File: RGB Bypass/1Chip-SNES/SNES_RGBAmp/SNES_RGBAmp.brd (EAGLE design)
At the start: 31.1 x 22.4 mm, 32 parts

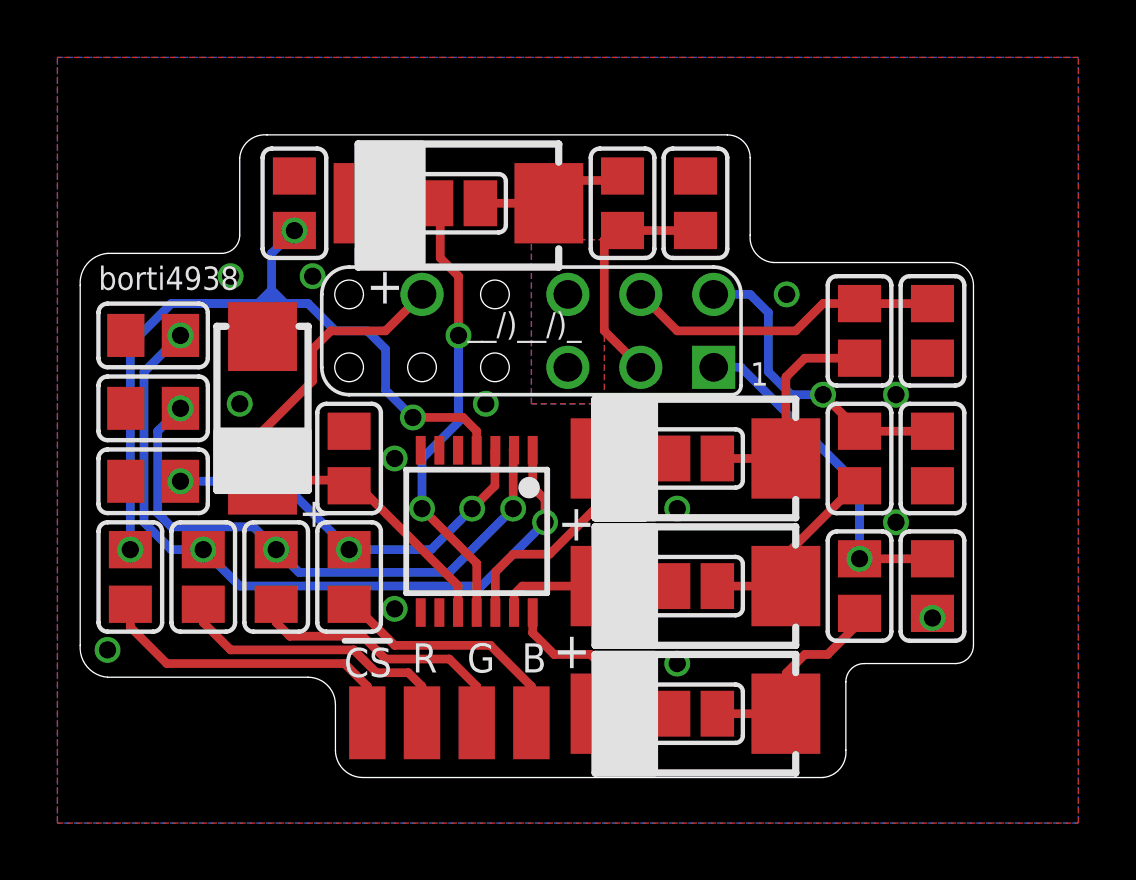
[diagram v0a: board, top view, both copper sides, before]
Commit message: rename folders a bit, add thermals to GND pads
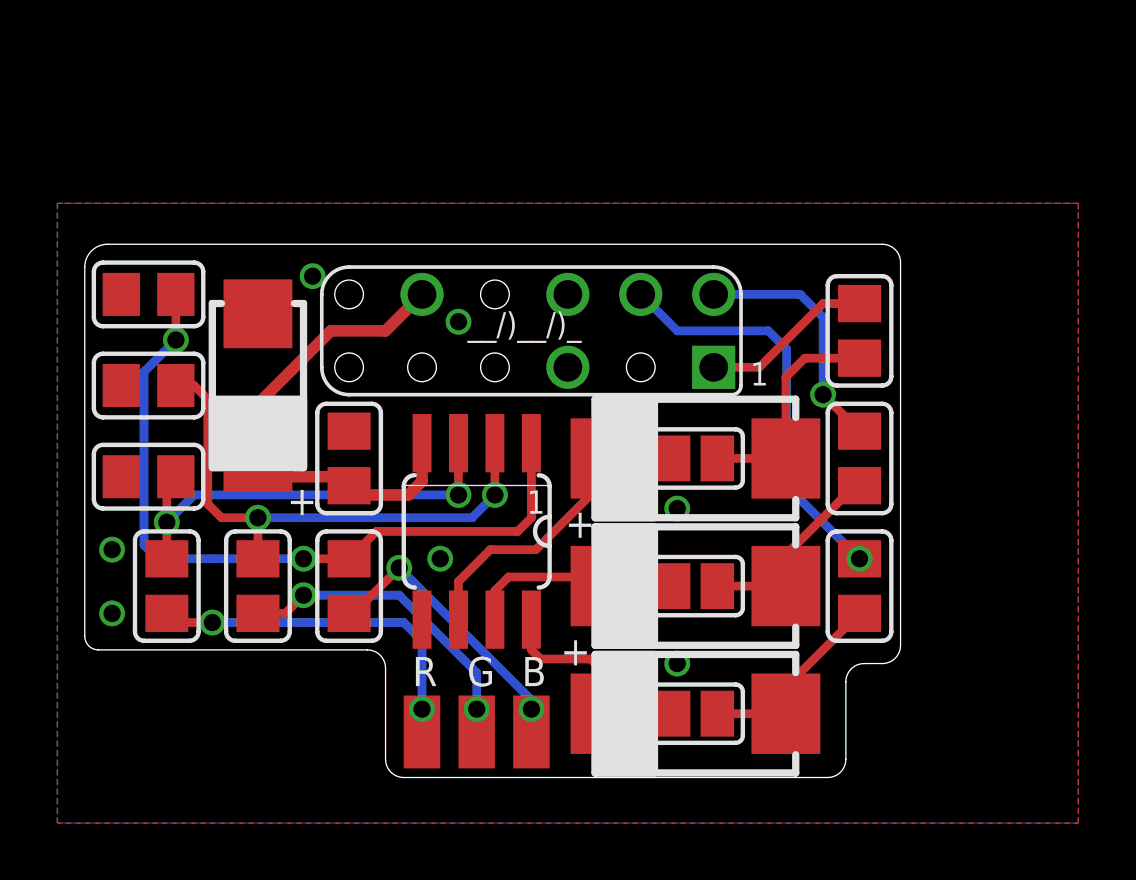
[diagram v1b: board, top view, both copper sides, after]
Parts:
- removed C10, C7, C8, C9: 47p, snescart:Z0805
- removed C6: 330u, rcl:SMC_D
- removed CS: (no value), wirepad:SMD1,27-2,54
- removed R10: 75-421, snescart:Z0805
- removed R11: 5.0k, snescart:Z0805
- removed R12: 4.3k, snescart:Z0805
- removed SJ4: (no value), jumper:SJ
- removed U$3: SNES_MULTIAV_RGBC_ONLY, snes_div:SNES_MULTIAV_RGBC_ONLY
- added U$1: THS7314, snescart:THS7314
- U$2: value THS7374 -> SNES_MULTIAV_RGB_ONLY; device snes_div:THS7374 -> snes_div:SNES_MULTIAV_RGB_ONLY
- moved R1 8.89 mm to (38.1, 38.7)
- moved R3 8.89 mm to (38.1, 29.8)
- moved U$2 7.24 mm to (26.7, 38.7), turned to 0 degrees
- moved R9 6.51 mm to (13.3, 40.0)
- moved R7 4.92 mm to (13.3, 33.7)
- moved R4 1.31 mm to (14.0, 29.8)
- moved C2 0.81 mm to (17.1, 36.8)
- moved R8 0.81 mm to (13.3, 36.8)
- moved R5 0.71 mm to (17.1, 29.8)
- moved R6 0.32 mm to (20.3, 29.8)
- moved B 0.32 mm to (26.7, 24.8)
- moved G 0.32 mm to (24.8, 24.8)
- moved R 0.32 mm to (22.9, 24.8)
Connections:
- removed net N$10: R11.1, R12.2, U$2.4
- removed net N$17: CS.1, R11.2
- removed net N$18: C6.+, SJ4.1, U$2.11
- removed net N$19: C6.-, R10.1, SJ4.2
- removed net N$20: C10.1, R10.2, U$3.P$3
- removed net R9: R6.1, R9.2, U$2.3
- new net N$3: R4.1, R7.2, U$1.3
- net GND: now also U$1.5, U$2.P$5, U$2.P$6; no longer C10.2, C7.2, C8.2, C9.2, R12.1, U$2.5, U$2.6, U$2.9, U$3.P$5, U$3.P$6
- net N$1: now also R6.1, R9.2, U$1.1; no longer R4.1, R7.2, U$2.1
- net N$11: now also U$1.6; no longer U$2.12
- net N$12: now also U$1.8; no longer U$2.14
- net N$2: now also U$1.2; no longer U$2.2
- net N$4: now also R3.1; no longer R1.1
- net N$5: now also R3.2, U$2.P$4; no longer C7.1, R1.2, U$3.P$1
- net N$6: now also U$2.P$2; no longer C8.1, U$3.P$2
- net N$7: now also U$1.7; no longer U$2.13
- net N$8: now also R1.1; no longer R3.1
- net N$9: now also R1.2, U$2.P$1; no longer C9.1, R3.2, U$3.P$4
- net VCC: now also U$1.4, U$2.P$10; no longer U$2.10, U$3.P$10
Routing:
- net N$10: track 27.6 -> 0.00 mm, vias 3 -> 0
- net N$18: track 18.3 -> 0.00 mm, vias 2 -> 0
- net N$3: track 0.00 -> 16.0 mm, vias 0 -> 2
- net R9: track 14.8 -> 0.00 mm, vias 3 -> 0
- net N$17: track 11.2 -> 0.00 mm
- net N$20: track 8.22 -> 0.00 mm
- net N$19: track 5.80 -> 0.00 mm
- net N$9: track 11.1 -> 6.00 mm
- net VCC: track 20.5 -> 17.7 mm
- net N$16: track 10.4 -> 13.1 mm, vias 0 -> 2
- net N$5: track 11.9 -> 14.2 mm
- net N$6: track 10.8 -> 8.64 mm
- net N$2: track 20.3 -> 18.7 mm, vias 3 -> 2
- net N$7: track 6.31 -> 7.56 mm
- net N$15: track 9.81 -> 11.1 mm, vias 0 -> 2
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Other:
- board size 31.1 x 22.4 mm -> 28.4 x 18.6 mm
- board text added: "C1 (22uF/ 6.3V )"
- board text added: "R1-R3 (NTSC:75Ω ,PAL:39Ω)"
- board text added: "RGBAmp for SNES V3.4"
- board text added: "THS 7314"
- board text removed: "(4.3kΩ)"
- board text removed: "(5.0kΩ)"
- board text removed: "(75Ω- 421Ω)"
- board text removed: "C1 (22uF/ 6.3V)"
- board text removed: "C10 (47pF)"
- board text removed: "C6 (330uF/ 6.3V )"
- board text removed: "C7-C9 (47pF) (Jr./Mini only)"
- board text removed: "R1-R3 (75Ω, PAL:39Ω)"
- board text removed: "R10"
- board text removed: "R11"
- board text removed: "R12"
- board text removed: "RGBAmp for SNES V3.3b"
- board text removed: "THS 7374"
- board text removed: "borti4938"
